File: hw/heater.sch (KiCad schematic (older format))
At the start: 9 parts, among them Q801 VNB35NV04TR-E, U802 VN5E010AH, U803 VN5E010AH

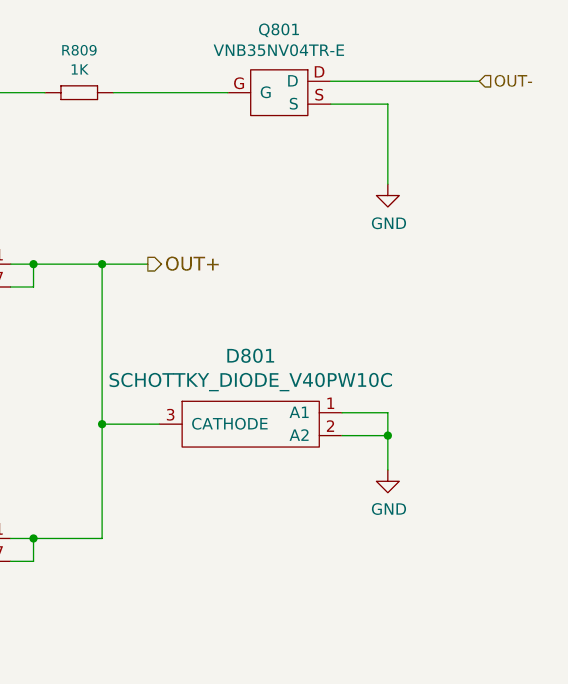
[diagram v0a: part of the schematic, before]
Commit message: 4.1.0 pcb ordered, with modified flyback diodes
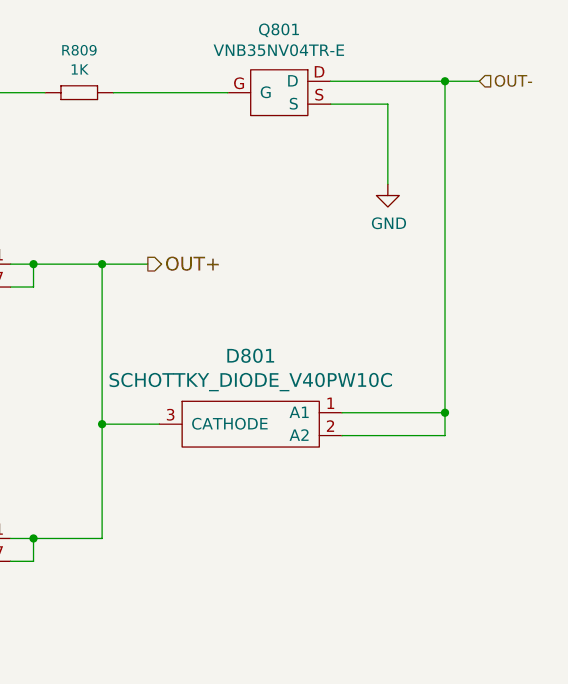
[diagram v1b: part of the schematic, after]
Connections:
- net GND: no longer D801.1 (A1), D801.2 (A2)
- net OUT-: now also D801.1 (A1), D801.2 (A2)
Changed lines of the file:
@@
 	-1   0    0    -1
 $EndComp
-$Comp
-L fsb-rescue:GND #PWR0807
-U 1 1 5A394BA1
-P 8300 4600
-F 0 "#PWR0807" H 8300 4350 50  0001 C CNN
-F 1 "GND" H 8305 4427 50  0000 C CNN
-F 2 "" H 8300 4600 50  0000 C CNN
-F 3 "" H 8300 4600 50  0000 C CNN
-	1    8300 4600
-	1    0    0    -1
-$EndComp
-Wire Wire Line
-	8300 4350 8300 4450
-Wire Wire Line
-	8300 4450 8100 4450
-Wire Wire Line
-	8300 4350 8100 4350
-Connection ~ 8300 4450
 Wire Wire Line
 	6750 3700 7050 3700
@@
 Wire Wire Line
 	4500 3700 4650 3700
-Wire Wire Line
-	8300 4450 8300 4600
 Text HLabel 6600 2950 0    50   Input ~ 0
 IN_PWM
@@
 OUT-
 Wire Wire Line
-	8700 2900 8050 2900
+	8700 2900 8550 2900
 $Comp
 L fsb-rescue:GND #PWR0107
@@
 Wire Wire Line
 	7300 4400 7050 4400
+Wire Wire Line
+	8550 2900 8550 4350
+Wire Wire Line
+	8550 4350 8100 4350
+Connection ~ 8550 2900
+Wire Wire Line
+	8550 2900 8050 2900
+Wire Wire Line
+	8100 4450 8550 4450
+Wire Wire Line
+	8550 4450 8550 4350
+Connection ~ 8550 4350
 $EndSCHEMATC

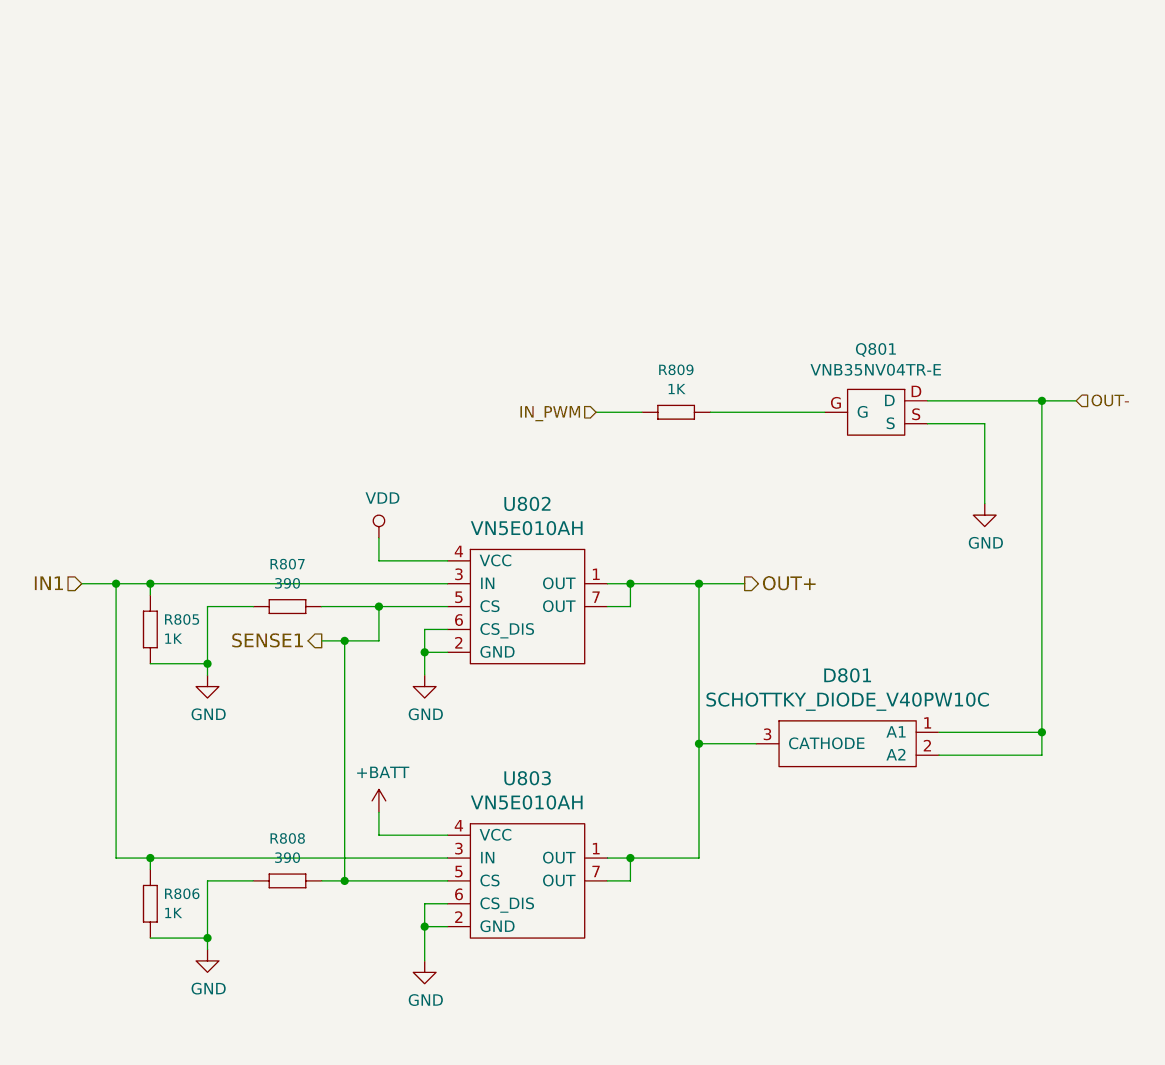
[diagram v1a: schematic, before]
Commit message: pcb with heater push-pull control circuit
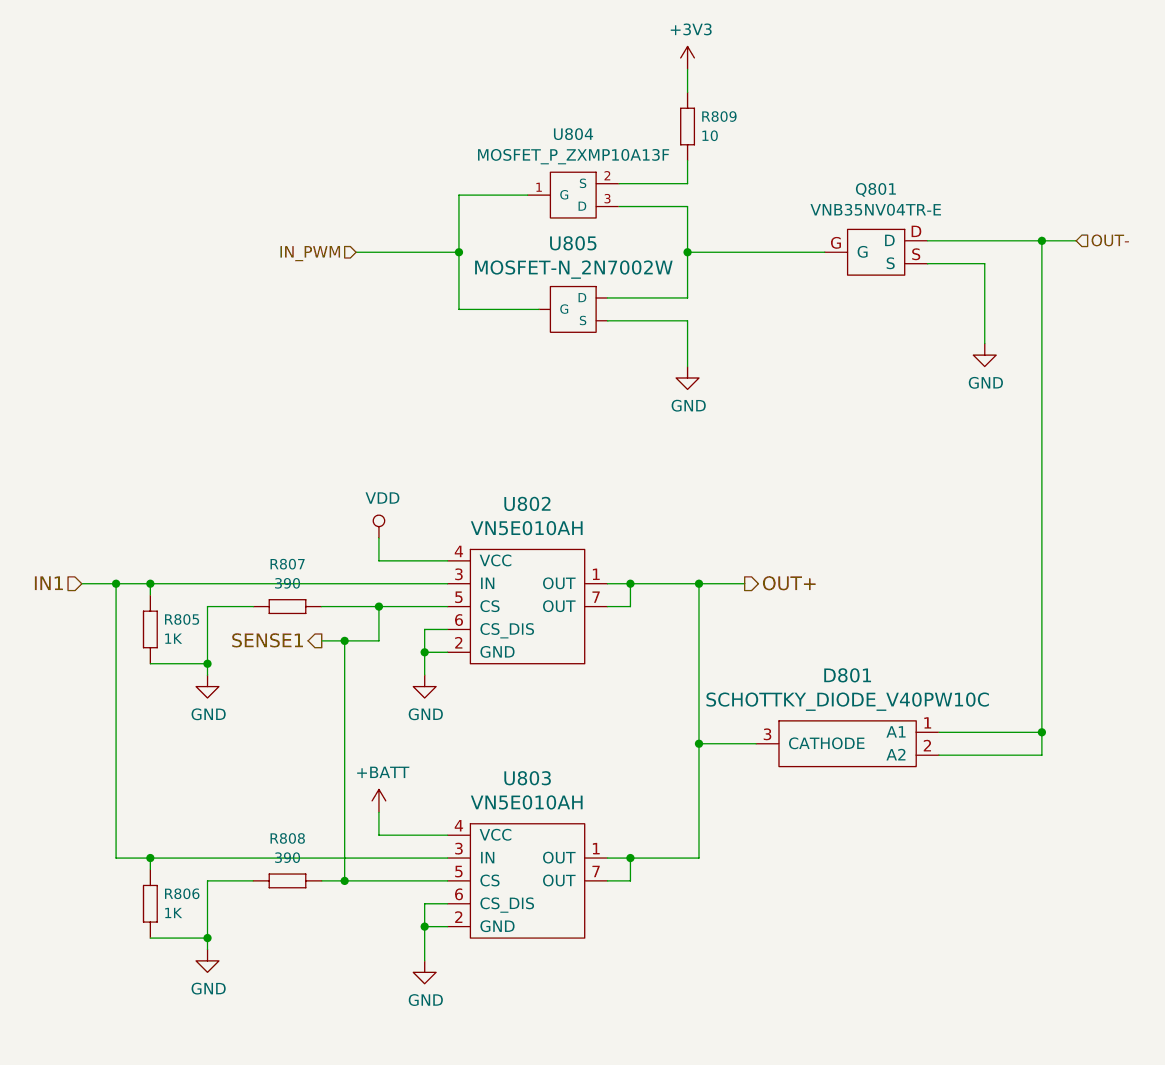
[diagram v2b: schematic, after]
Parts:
- removed R809: 1K, yageo:0603, symbol fsb-rescue:1K
- added R809: 10, yageo:0603, symbol yageo:10
- added U804: MOSFET_P_ZXMP10A13F, usevolt:SOT-23_3-PIN, symbol usevolt:MOSFET_P_ZXMP10A13F
- added U805: MOSFET-N_2N7002W, usevolt:SOT323, symbol usevolt:MOSFET-N_2N7002W
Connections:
- net GND: now also U805.R (S)
- net IN_PWM: now also U804.1 (G), U805.L (G)
- net at Q801.G: now also U804.3 (D), U805.M (D)
- new net: R809.1 (R1), U804.2 (S)
- new net +3V3: R809.2 (R2)
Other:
- moved on the sheet: Q801
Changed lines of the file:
@@
 Wire Wire Line
 	4500 3700 4650 3700
-Text HLabel 6600 2950 0    50   Input ~ 0
+Text HLabel 5550 2250 0    50   Input ~ 0
 IN_PWM
 $Comp
 L usevolt:VNB35NV04TR-E Q801
 U 1 1 5ABB9BC8
-P 7850 2950
-F 0 "Q801" H 7825 3225 50  0000 C CNN
-F 1 "VNB35NV04TR-E" H 7825 3134 50  0000 C CNN
-F 2 "usevolt:D2" H 7600 2950 50  0001 C CNN
-F 3 "http://www.st.com/content/ccc/resource/technical/document/datasheet/95/6b/79/42/8e/45/4a/e6/DM00062289.pdf/files/DM00062289.pdf/jcr:content/translations/en.DM00062289.pdf" H 7600 2950 50  0001 C CNN
-F 4 "STMicroelectronics" H 7950 3200 50  0001 C CNN "Manufacturer"
-F 5 "VNB35NV04TR-E" H 8050 3300 50  0001 C CNN "Manufacturer Part Number"
-F 6 "Digikey" H 8150 3400 50  0001 C CNN "1st Source"
-F 7 "497-11686-1-ND" H 8250 3500 50  0001 C CNN "1st Source Part Number"
-F 8 "Mouser" H 8350 3600 50  0001 C CNN "2nd Source"
-F 9 "511-VNB35NV04TR-E" H 8450 3700 50  0001 C CNN "2nd Source Part Number"
-	1    7850 2950
+P 7850 2250
+F 0 "Q801" H 7825 2525 50  0000 C CNN
+F 1 "VNB35NV04TR-E" H 7825 2434 50  0000 C CNN
+F 2 "usevolt:D2" H 7600 2250 50  0001 C CNN
+F 3 "http://www.st.com/content/ccc/resource/technical/document/datasheet/95/6b/79/42/8e/45/4a/e6/DM00062289.pdf/files/DM00062289.pdf/jcr:content/translations/en.DM00062289.pdf" H 7600 2250 50  0001 C CNN
+F 4 "STMicroelectronics" H 7950 2500 50  0001 C CNN "Manufacturer"
+F 5 "VNB35NV04TR-E" H 8050 2600 50  0001 C CNN "Manufacturer Part Number"
+F 6 "Digikey" H 8150 2700 50  0001 C CNN "1st Source"
+F 7 "497-11686-1-ND" H 8250 2800 50  0001 C CNN "1st Source Part Number"
+F 8 "Mouser" H 8350 2900 50  0001 C CNN "2nd Source"
+F 9 "511-VNB35NV04TR-E" H 8450 3000 50  0001 C CNN "2nd Source Part Number"
+	1    7850 2250
 	1    0    0    -1
 $EndComp
-Text HLabel 8700 2900 2    50   Input ~ 0
+Text HLabel 8700 2200 2    50   Input ~ 0
 OUT-
 Wire Wire Line
-	8700 2900 8550 2900
+	8700 2200 8550 2200
 $Comp
 L fsb-rescue:GND #PWR0107
 U 1 1 5ABBA8C9
-P 8300 3350
-F 0 "#PWR0107" H 8300 3100 50  0001 C CNN
-F 1 "GND" H 8305 3177 50  0000 C CNN
-F 2 "" H 8300 3350 50  0000 C CNN
-F 3 "" H 8300 3350 50  0000 C CNN
-	1    8300 3350
+P 8300 2650
+F 0 "#PWR0107" H 8300 2400 50  0001 C CNN
+F 1 "GND" H 8305 2477 50  0000 C CNN
+F 2 "" H 8300 2650 50  0000 C CNN
+F 3 "" H 8300 2650 50  0000 C CNN
+	1    8300 2650
 	1    0    0    -1
 $EndComp
 Wire Wire Line
-	8300 3350 8300 3000
+	8300 2650 8300 2300
 Wire Wire Line
-	8300 3000 8050 3000
-$Comp
-L fsb-rescue:1K R809
-U 1 1 5ABBC1B6
-P 6900 2950
-F 0 "R809" H 6950 3134 45  0000 C CNN
-F 1 "1K" H 6950 3050 45  0000 C CNN
-F 2 "yageo:0603" H 6930 3100 20  0001 C CNN
-F 3 "" H 6869 2989 60  0001 C CNN
-F 4 "Digikey" H 7169 3289 60  0001 C CNN "1st Source"
-F 5 "RC0603FR-071KL" H 7069 3189 60  0001 C CNN "Manufacturer Part Number"
-F 6 "YAGEO" H 6969 3089 60  0001 C CNN "Manufacturer"
-	1    6900 2950
-	1    0    0    -1
-$EndComp
-Wire Wire Line
-	6800 2950 6600 2950
-Wire Wire Line
-	7100 2950 7600 2950
+	8300 2300 8050 2300
 Wire Wire Line
 	7050 4400 7050 3700
@@
 	7300 4400 7050 4400
 Wire Wire Line
-	8550 2900 8550 4350
+	8550 2200 8550 4350
 Wire Wire Line
 	8550 4350 8100 4350
-Connection ~ 8550 2900
+Connection ~ 8550 2200
 Wire Wire Line
-	8550 2900 8050 2900
+	8550 2200 8050 2200
 Wire Wire Line
 	8100 4450 8550 4450
@@
 	8550 4450 8550 4350
 Connection ~ 8550 4350
+$Comp
+L usevolt:MOSFET-N_2N7002W U805
+U 1 1 5B408B19
+P 6500 2500
+F 0 "U805" H 6500 2787 60  0000 C CNN
+F 1 "MOSFET-N_2N7002W" H 6500 2681 60  0000 C CNN
+F 2 "usevolt:SOT323" H 6800 3400 60  0001 C CNN
+F 3 "http://www.onsemi.com/pub_link/Collateral/2N7002W-D.PDF" H 6650 3500 60  0001 C CNN
+F 4 "2533171" H 7075 3325 60  0001 C CNN "2nd Source Part Number"
+F 5 "2N7002WT1G" H 6675 2925 60  0001 C CNN "Manufacturer Part Number"
+F 6 "2N7002WT1GOSCT-ND" H 6875 3125 60  0001 C CNN "1st Source Part Number"
+F 7 "Digikey" H 6775 3025 60  0001 C CNN "1st Source"
+F 8 "Farnell" H 6975 3225 60  0001 C CNN "2nd Source"
+F 9 "ON Semiconductor" H 6575 2825 60  0001 C CNN "Manufacturer"
+	1    6500 2500
+	1    0    0    -1
+$EndComp
+$Comp
+L usevolt:MOSFET_P_ZXMP10A13F U804
+U 1 1 5B408DAE
+P 6500 2000
+F 0 "U804" H 6500 2265 50  0000 C CNN
+F 1 "MOSFET_P_ZXMP10A13F" H 6500 2174 50  0000 C CNN
+F 2 "usevolt:SOT-23_3-PIN" H 6500 2200 50  0001 C CNN
+F 3 "http://www.farnell.com/datasheets/1915646.pdf?_ga=2.76885333.1768503822.1530426090-1862443086.1504075057" H 6500 2200 50  0001 C CNN
+F 4 "DIODES INC." H 6600 2250 50  0001 C CNN "Manufacturer"
+F 5 "ZXMP10A13FTA" H 6700 2350 50  0001 C CNN "Manufacturer Part Number"
+F 6 "Farnell" H 6800 2450 50  0001 C CNN "1st Source"
+F 7 "1843777" H 6900 2550 50  0001 C CNN "1st Source Part Number"
+	1    6500 2000
+	1    0    0    -1
+$EndComp
+Wire Wire Line
+	6300 2000 6000 2000
+Wire Wire Line
+	6000 2000 6000 2250
+Wire Wire Line
+	6000 2500 6350 2500
+Wire Wire Line
+	5550 2250 6000 2250
+Connection ~ 6000 2250
+Wire Wire Line
+	6000 2250 6000 2500
+$Comp
+L fsb-rescue:GND #PWR0109
+U 1 1 5B40D98A
+P 7000 2750
+F 0 "#PWR0109" H 7000 2500 50  0001 C CNN
+F 1 "GND" H 7005 2577 50  0000 C CNN
+F 2 "" H 7000 2750 50  0000 C CNN
+F 3 "" H 7000 2750 50  0000 C CNN
+	1    7000 2750
+	1    0    0    -1
+$EndComp
+Wire Wire Line
+	7000 2750 7000 2550
+Wire Wire Line
+	7000 2550 6650 2550
+$Comp
+L yageo:10 R809
+U 1 1 5B410B23
+P 7000 1650
+F 0 "R809" V 7008 1708 45  0000 L CNN
+F 1 "10" V 7092 1708 45  0000 L CNN
+F 2 "yageo:0603" H 7030 1800 20  0001 C CNN
+F 3 "" H 6969 1689 60  0001 C CNN
+F 4 "" H 7369 2089 60  0001 C CNN "1st Source Part Number"
+F 5 "Digikey" H 7269 1989 60  0001 C CNN "1st Source"
+F 6 "RC0603FR-0710RL" H 7169 1889 60  0001 C CNN "Manufacturer Part Number"
+F 7 "YAGEO" H 7069 1789 60  0001 C CNN "Manufacturer"
+	1    7000 1650
+	0    1    1    0
+$EndComp
+Wire Wire Line
+	7000 1550 7000 1450
+Wire Wire Line
+	7000 1850 7000 1950
+Wire Wire Line
+	7000 1950 6700 1950
+Wire Wire Line
+	6700 2050 7000 2050
+Wire Wire Line
+	7000 2050 7000 2250
+Wire Wire Line
+	7000 2250 7600 2250
+Wire Wire Line
+	7000 2250 7000 2450
+Wire Wire Line
+	7000 2450 6650 2450
+Connection ~ 7000 2250
+$Comp
+L fsb-rescue:+3V3 #PWR0110
+U 1 1 5B415F3E
+P 7000 1450
+F 0 "#PWR0110" H 7000 1300 50  0001 C CNN
+F 1 "+3V3" H 7015 1623 50  0000 C CNN
+F 2 "" H 7000 1450 50  0000 C CNN
+F 3 "" H 7000 1450 50  0000 C CNN
+	1    7000 1450
+	1    0    0    -1
+$EndComp
 $EndSCHEMATC

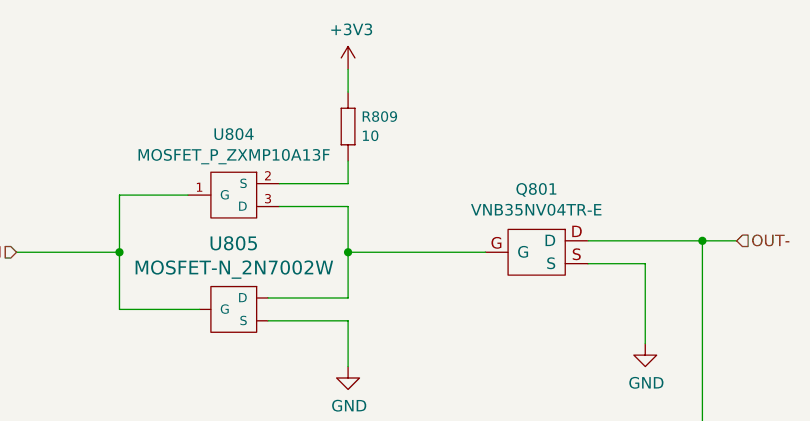
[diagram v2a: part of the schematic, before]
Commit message: variable heater speed working
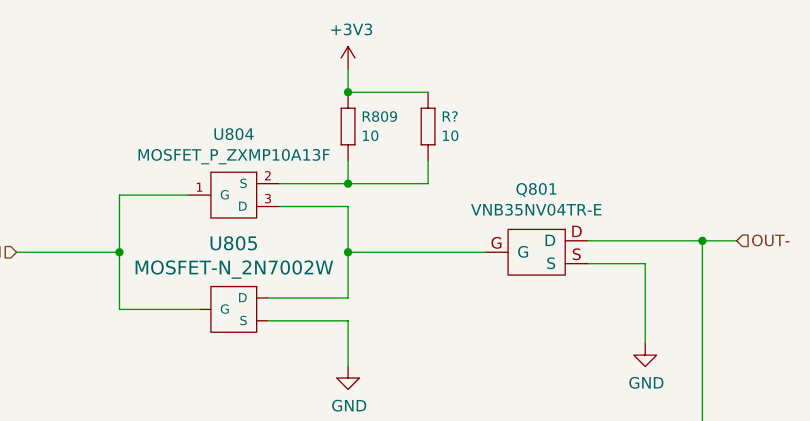
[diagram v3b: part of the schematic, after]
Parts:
- added R?: 10, yageo:0603, symbol yageo:10
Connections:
- net +3V3: now also R?.2 (R2)
- net at R809.1 (R1), U804.2 (S): now also R?.1 (R1)
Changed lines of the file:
@@
 Wire Wire Line
 	7000 2550 6650 2550
-$Comp
-L yageo:10 R809
-U 1 1 5B410B23
-P 7000 1650
-F 0 "R809" V 7008 1708 45  0000 L CNN
-F 1 "10" V 7092 1708 45  0000 L CNN
-F 2 "yageo:0603" H 7030 1800 20  0001 C CNN
-F 3 "" H 6969 1689 60  0001 C CNN
-F 4 "" H 7369 2089 60  0001 C CNN "1st Source Part Number"
-F 5 "Digikey" H 7269 1989 60  0001 C CNN "1st Source"
-F 6 "RC0603FR-0710RL" H 7169 1889 60  0001 C CNN "Manufacturer Part Number"
-F 7 "YAGEO" H 7069 1789 60  0001 C CNN "Manufacturer"
-	1    7000 1650
-	0    1    1    0
-$EndComp
 Wire Wire Line
 	7000 1550 7000 1450
@@
 	1    0    0    -1
 $EndComp
+$Comp
+L yageo:10 R809
+U 1 1 5B410B23
+P 7000 1650
+F 0 "R809" V 7008 1708 45  0000 L CNN
+F 1 "10" V 7092 1708 45  0000 L CNN
+F 2 "yageo:0603" H 7030 1800 20  0001 C CNN
+F 3 "" H 6969 1689 60  0001 C CNN
+F 4 "" H 7369 2089 60  0001 C CNN "1st Source Part Number"
+F 5 "Digikey" H 7269 1989 60  0001 C CNN "1st Source"
+F 6 "RC0603FR-0710RL" H 7169 1889 60  0001 C CNN "Manufacturer Part Number"
+F 7 "YAGEO" H 7069 1789 60  0001 C CNN "Manufacturer"
+	1    7000 1650
+	0    1    1    0
+$EndComp
+$Comp
+L yageo:10 R?
+U 1 1 5B5E9327
+P 7350 1650
+F 0 "R?" V 7358 1708 45  0000 L CNN
+F 1 "10" V 7442 1708 45  0000 L CNN
+F 2 "yageo:0603" H 7380 1800 20  0001 C CNN
+F 3 "" H 7319 1689 60  0001 C CNN
+F 4 "" H 7719 2089 60  0001 C CNN "1st Source Part Number"
+F 5 "Digikey" H 7619 1989 60  0001 C CNN "1st Source"
+F 6 "RC0603FR-0710RL" H 7519 1889 60  0001 C CNN "Manufacturer Part Number"
+F 7 "YAGEO" H 7419 1789 60  0001 C CNN "Manufacturer"
+	1    7350 1650
+	0    1    1    0
+$EndComp
+Wire Wire Line
+	7350 1550 7000 1550
+Connection ~ 7000 1550
+Wire Wire Line
+	7350 1850 7350 1950
+Wire Wire Line
+	7350 1950 7000 1950
+Connection ~ 7000 1950
 $EndSCHEMATC
